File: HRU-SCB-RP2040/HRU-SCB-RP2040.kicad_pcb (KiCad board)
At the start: 2 copper layers, 42 x 55 mm, 51 parts, among them J1 Pico_Socket_B, J2 Pico_Socket_A, J3 GROVE-CONNECTOR-DIP_4P-2.0_, J4 Conn_01x02_Pin, U1 MAX485E, U2 MAX485E, U3 R-78E3.3-0.5

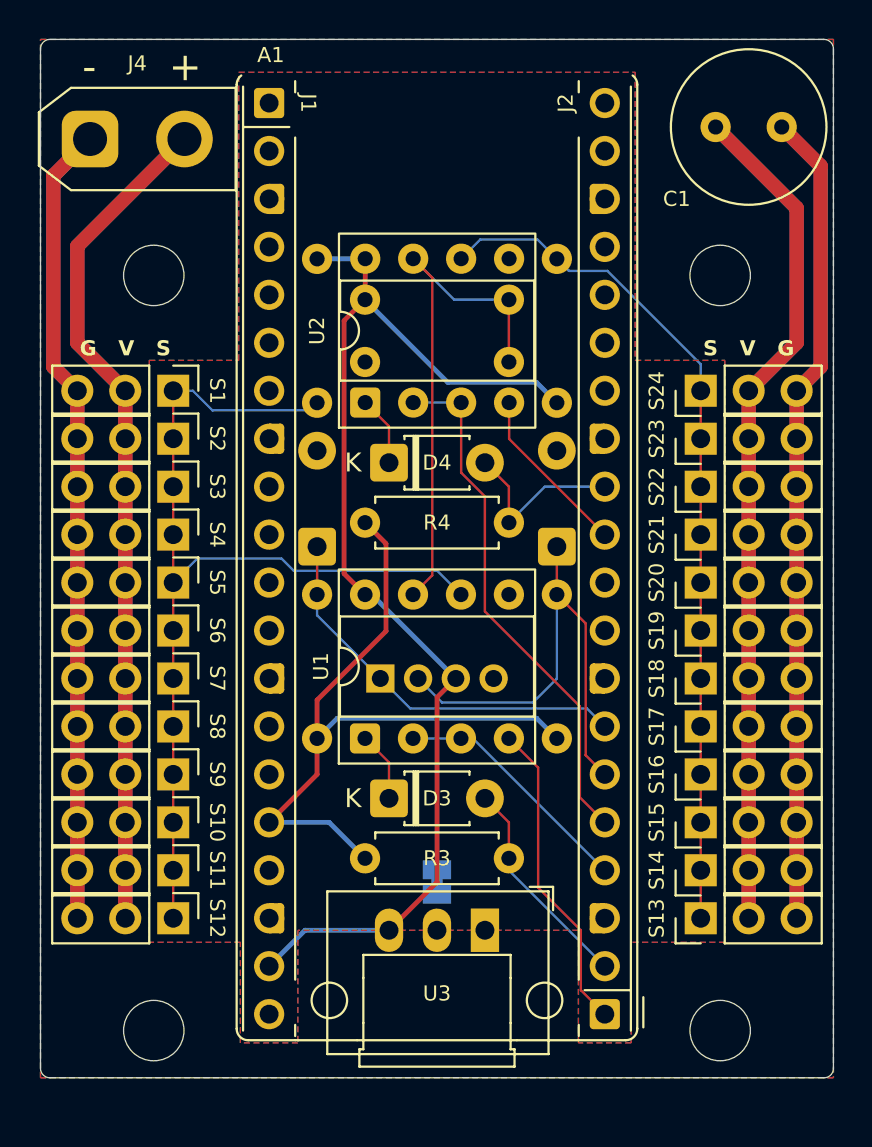
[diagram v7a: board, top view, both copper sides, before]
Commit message: fix(HRU-SCB-RP2040): assign 3V3 to I2C's VCC and refactor parts layout
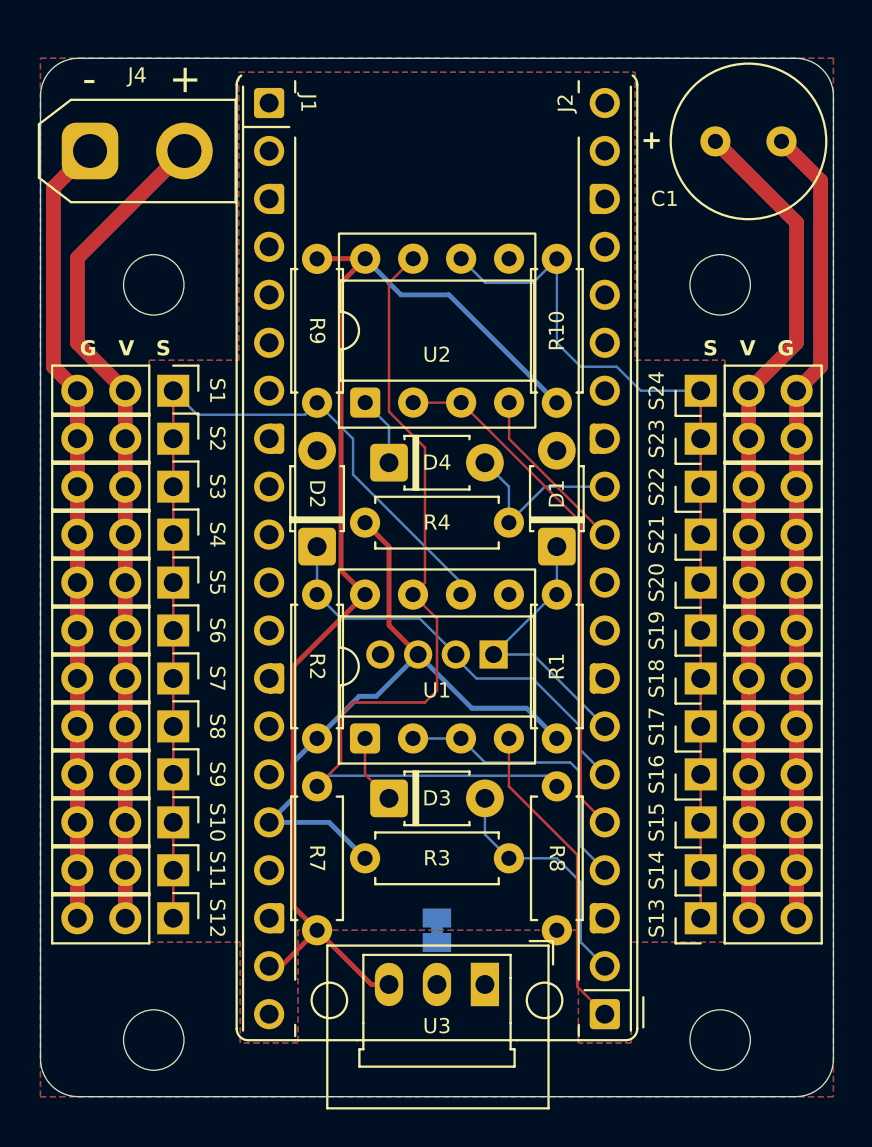
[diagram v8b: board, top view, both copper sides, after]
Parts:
- D1, D2, R1, R10, R2, R7, R8, R9: moved to F.Cu
- moved R7 33.5 mm to (143.7, 142.2), turned to 90 degrees
- moved R8 22.6 mm to (156.3, 134.6), turned to -90 degrees
- moved D1 12.7 mm to (156.3, 121.9)
- moved D2 12.7 mm to (143.7, 121.9)
- moved R1 12.7 mm to (156.3, 124.4)
- moved R2 12.7 mm to (143.7, 124.4)
- moved U3 2.87 mm to (152.5, 145.1)
- moved JP1 2.56 mm to (150.0, 142.2)
- moved REF** 1.55 mm to (155.3, 148.2)
- moved J3 1.27 mm to (150.0, 127.6), turned to 180 degrees
- moved C1 0.76 mm to (164.8, 100.4)
- moved J4 0.63 mm to (131.6, 100.9)
- moved H1 0.50 mm to (135.0, 108.0)
- moved H2 0.50 mm to (135.0, 148.0)
- moved H3 0.50 mm to (165.0, 148.0)
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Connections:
- J3 pad 3: +5V -> +3V3
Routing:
- net /ServoPort/SERVO.NULL: track 27.9 -> 48.1 mm
- net /I2C0.SCL: track 21.3 -> 14.7 mm
- net /I2C0.SDA: track 26.0 -> 22.6 mm
- net /ServoPort/SERVO.SERIAL0: track 52.7 -> 49.7 mm
- net GNDPWR: track 171.8 -> 169.0 mm
- net VCC: track 178.8 -> 176.0 mm
- net +3V3: track 38.3 -> 35.9 mm
- net /SERVO.SERIAL0.DE: track 13.1 -> 15.3 mm
- net /ServoPort/SERVO.SERIAL1: track 45.2 -> 47.2 mm
- net /SERVO.SERIAL0.RX: track 11.5 -> 13.0 mm
- net +5V: track 62.3 -> 62.9 mm
- net /SERVO.SERIAL1.TX: track 9.10 -> 9.73 mm
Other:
- outline, holes or cut-outs redrawn
- board text added: "+"
